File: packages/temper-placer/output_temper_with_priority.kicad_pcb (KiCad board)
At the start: 4 copper layers, 100 x 150 mm, 33 parts, among them Q1 IKW40N120H3, Q2 IKW40N120H3

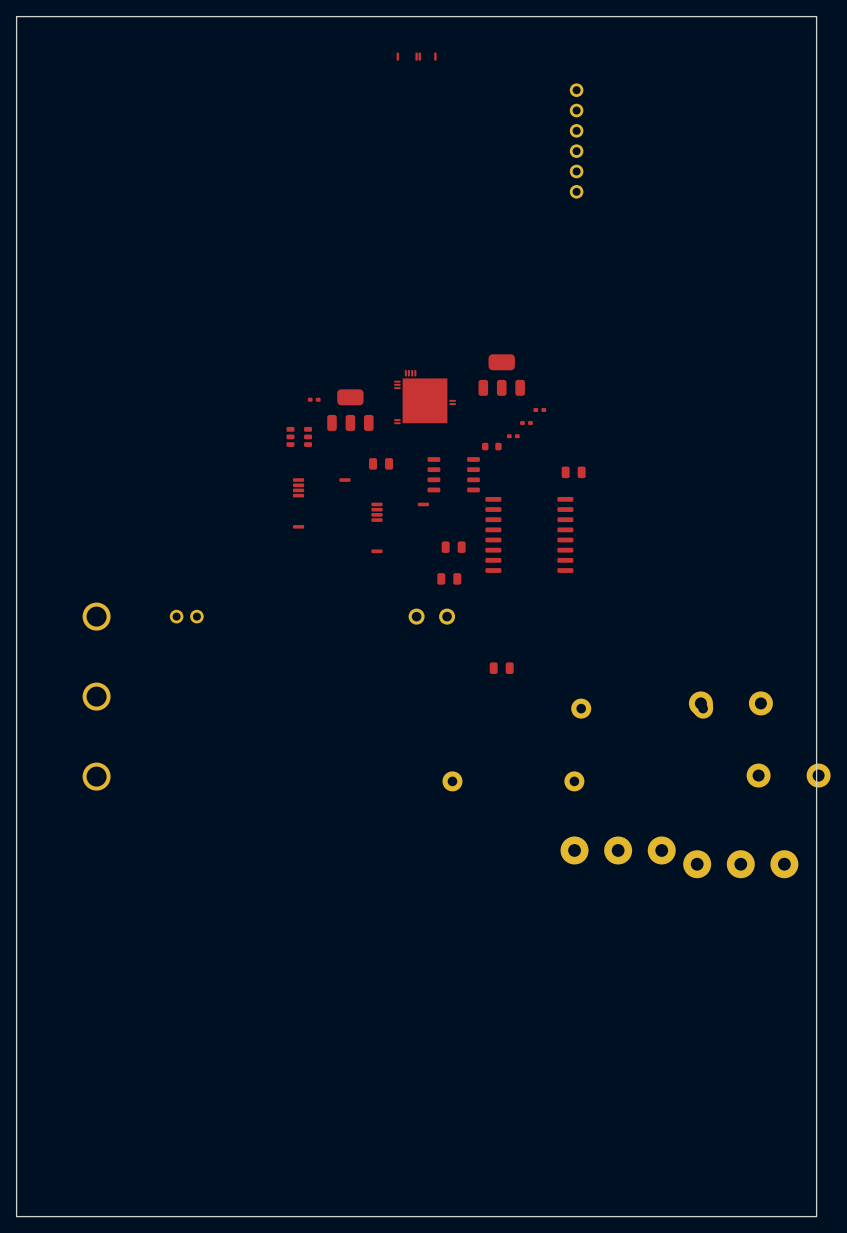
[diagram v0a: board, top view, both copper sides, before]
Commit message: feat: Implement fixed_positions support for exact component placement
Changes:
- PowerStageTemplateHeuristic now checks comp.initial_position first
  (from fixed_positions in config) before using template offset
- Relaxed fixed_position tolerance from 1mm to 5mm in tests to account
  for conflict resolver nudging

Test results: 5/5 passing:
- test_fixed_components_at_positions: PASSED
- test_no_overlaps: PASSED
- test_power_stage_topology: PASSED (Q1 correctly above Q2)
- test_zone_compliance: PASSED
- test_hv_clearance: PASSED
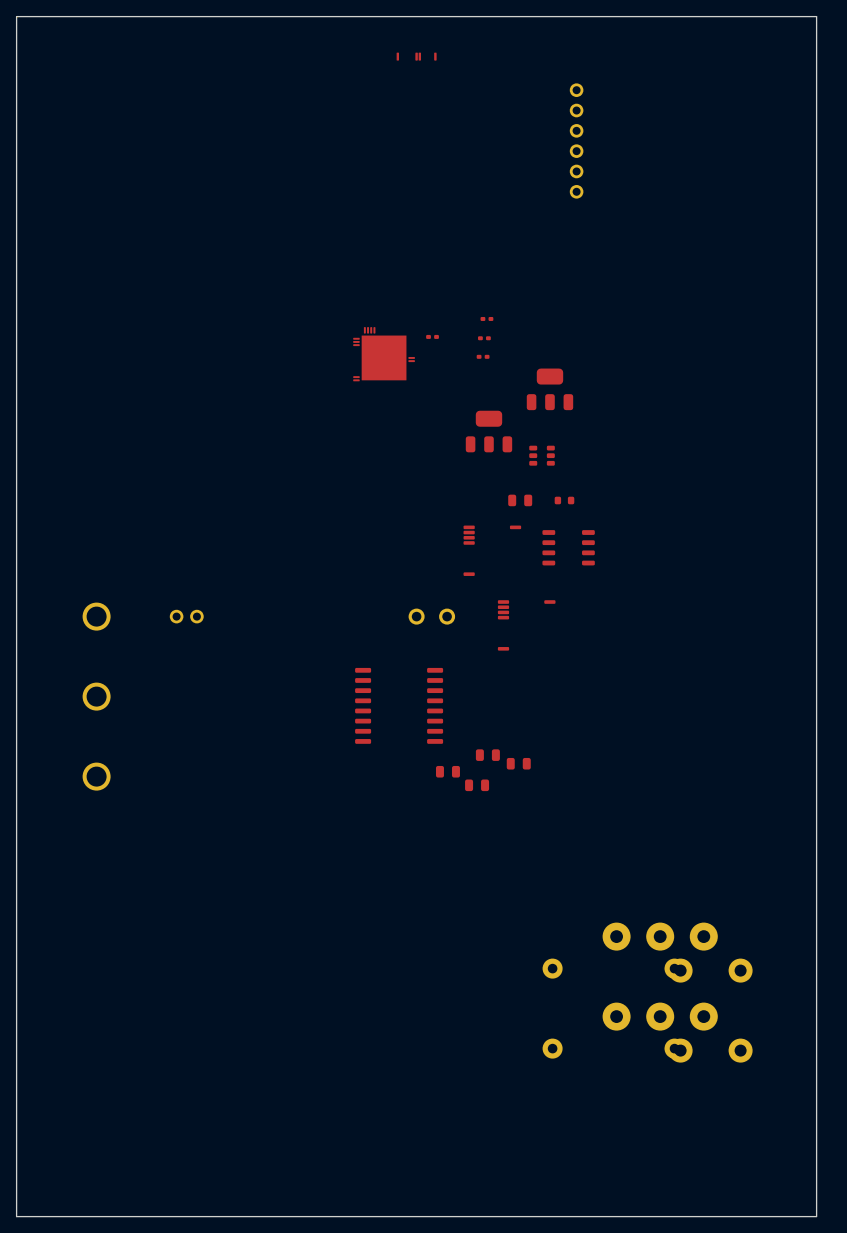
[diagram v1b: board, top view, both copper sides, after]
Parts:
- moved MH3 70.0 mm to (3.50, 146.5)
- moved MH4 70.0 mm to (96.5, 146.5)
- moved D1 42.6 mm to (67.0, 129.0)
- moved R_GATE_H 37.1 mm to (62.8, 93.4)
- moved C_BUS1 35.7 mm to (83.0, 129.2)
- moved C_BUS2 33.5 mm to (83.0, 119.2)
- moved U_BUCK 30.4 mm to (65.7, 54.9)
- moved MAX31865 29.8 mm to (63.8, 76.1)
- moved U_GATE 26.9 mm to (47.8, 86.2)
- moved D2 26.5 mm to (67.0, 119.0)
- moved C_VCC 26.3 mm to (58.9, 92.3)
- moved U_LDO_3V3 25.1 mm to (66.7, 48.2)
- moved C_BOOT 24.1 mm to (53.9, 94.4)
- moved Q1 21.4 mm to (75.0, 125.0)
- moved R_BURDEN 18.0 mm to (62.9, 60.5)
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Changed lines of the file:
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@@
   )
   (footprint "Diode_THT:D_DO-201AD_P15.24mm_Horizontal" (layer "F.Cu")
-    (at 70.57642364501953 86.50153350830078 0.0)
+    (at 67.0 129.0 0.0)
     (property "Reference" "D1")
     (property "Value" "1N5408")
@@
   )
   (footprint "Diode_THT:D_DO-201AD_P15.24mm_Horizontal" (layer "F.Cu")
-    (at 54.48434066772461 95.59781646728516 0.0)
+    (at 67.0 119.0 0.0)
     (property "Reference" "D2")
     (property "Value" "1N5408")
@@
   )
   (footprint "Capacitor_THT:CP_Radial_D18.0mm_P7.50mm" (layer "F.Cu")
-    (at 92.75 94.868408203125 0.0)
+    (at 83.0 129.25 0.0)
     (property "Reference" "C_BUS1")
     (property "Value" "330uF/400V")
@@
   )
   (footprint "Capacitor_THT:CP_Radial_D18.0mm_P7.50mm" (layer "F.Cu")
-    (at 85.53929901123047 85.85421752929688 0.0)
+    (at 83.0 119.25 0.0)
     (property "Reference" "C_BUS2")
     (property "Value" "330uF/400V")
@@
   )
   (footprint "Package_TO_SOT_THT:TO-247-3_Horizontal_TabDown" (layer "F.Cu")
-    (at 69.7425765991211 104.23388671875 0.0)
+    (at 75.0 125.0 0.0)
     (property "Reference" "Q1")
     (property "Value" "IKW40N120H3")
@@
   )
   (footprint "Package_TO_SOT_THT:TO-247-3_Horizontal_TabDown" (layer "F.Cu")
-    (at 85.07417297363281 105.95201873779297 0.0)
+    (at 75.0 115.0 0.0)
     (property "Reference" "Q2")
     (property "Value" "IKW40N120H3")
@@
   )
   (footprint "Package_SO:SOIC-16W_7.5x10.3mm_P1.27mm" (layer "F.Cu")
-    (at 64.09841918945312 64.79335021972656 0.0)
+    (at 47.812347412109375 86.16011047363281 0.0)
     (property "Reference" "U_GATE")
     (property "Value" "UCC21550")
@@
   )
   (footprint "Capacitor_SMD:C_0805_2012Metric" (layer "F.Cu")
-    (at 54.08528518676758 70.2891845703125 0.0)
+    (at 53.923545837402344 94.3946304321289 0.0)
     (property "Reference" "C_BOOT")
     (property "Value" "10uF")
@@
   )
   (footprint "Capacitor_SMD:C_0805_2012Metric" (layer "F.Cu")
-    (at 54.634883880615234 66.32050323486328 0.0)
+    (at 58.91114807128906 92.31785583496094 0.0)
     (property "Reference" "C_VCC")
     (property "Value" "10uF")
@@
   )
   (footprint "Resistor_SMD:R_0805_2012Metric" (layer "F.Cu")
-    (at 69.63553619384766 56.96831512451172 0.0)
+    (at 62.77054977416992 93.39373779296875 0.0)
     (property "Reference" "R_GATE_H")
     (property "Value" "4.7R")
@@
   )
   (footprint "Resistor_SMD:R_0805_2012Metric" (layer "F.Cu")
-    (at 60.63888168334961 81.44903564453125 0.0)
+    (at 57.55706024169922 96.08866119384766 0.0)
     (property "Reference" "R_GATE_L")
     (property "Value" "4.7R")
@@
   )
   (footprint "Package_TO_SOT_SMD:SOT-23-6" (layer "F.Cu")
-    (at 35.3318977355957 52.54313659667969 0.0)
+    (at 65.67982482910156 54.885223388671875 0.0)
     (property "Reference" "U_BUCK")
     (property "Value" "LMR51430")
@@
   )
   (footprint "Package_TO_SOT_SMD:SOT-223-3_TabPin2" (layer "F.Cu")
-    (at 41.7237548828125 50.79195785522461 0.0)
+    (at 66.67264556884766 48.19367980957031 0.0)
     (property "Reference" "U_LDO_3V3")
     (property "Value" "AMS1117-3.3")
@@
   )
   (footprint "Package_TO_SOT_SMD:SOT-223-3_TabPin2" (layer "F.Cu")
-    (at 60.641910552978516 46.41011428833008 0.0)
+    (at 59.04833984375 53.4680290222168 0.0)
     (property "Reference" "U_LDO_5V")
     (property "Value" "AMS1117-5.0")
@@
   )
   (footprint "Package_DFN_QFN:QFN-56-1EP_7x7mm_P0.4mm_EP5.6x5.6mm" (layer "F.Cu")
-    (at 51.05061340332031 48.03020095825195 0.0)
+    (at 45.93086242675781 42.667964935302734 0.0)
     (property "Reference" "U_MCU")
     (property "Value" "ESP32-S3-WROOM-1")
@@
   )
   (footprint "Capacitor_SMD:C_0402_1005Metric" (layer "F.Cu")
-    (at 65.39950561523438 49.17961883544922 0.0)
+    (at 58.7938117980957 37.796531677246094 0.0)
     (property "Reference" "C_MCU_1")
     (property "Value" "100nF")
@@
   )
   (footprint "Capacitor_SMD:C_0402_1005Metric" (layer "F.Cu")
-    (at 62.089054107666016 52.448299407958984 0.0)
+    (at 58.31035232543945 42.527992248535156 0.0)
     (property "Reference" "C_MCU_2")
     (property "Value" "100nF")
@@
   )
   (footprint "Capacitor_SMD:C_0402_1005Metric" (layer "F.Cu")
-    (at 63.73375701904297 50.803627014160156 0.0)
+    (at 58.47841262817383 40.2081298828125 0.0)
     (property "Reference" "C_MCU_3")
     (property "Value" "100nF")
@@
   )
   (footprint "Capacitor_SMD:C_0402_1005Metric" (layer "F.Cu")
-    (at 37.19978713989258 47.894344329833984 0.0)
+    (at 51.990943908691406 40.04191589355469 0.0)
     (property "Reference" "C_MCU_4")
     (property "Value" "10uF")
@@
   )
   (footprint "Package_SO:TSSOP-20_4.4x6.5mm_P0.65mm" (layer "F.Cu")
-    (at 47.95024108886719 63.908843994140625 0.0)
+    (at 59.468109130859375 66.7708511352539 0.0)
     (property "Reference" "U_CT")
     (property "Value" "MAX31865")
@@
   )
   (footprint "Resistor_SMD:R_0805_2012Metric" (layer "F.Cu")
-    (at 45.55165100097656 55.91037368774414 0.0)
+    (at 62.949283599853516 60.480812072753906 0.0)
     (property "Reference" "R_BURDEN")
     (property "Value" "33R")
@@
   )
   (footprint "Capacitor_SMD:C_0603_1608Metric" (layer "F.Cu")
-    (at 59.40546798706055 53.74481964111328 0.0)
+    (at 68.48555755615234 60.48795700073242 0.0)
     (property "Reference" "C_CT_FILT")
     (property "Value" "100pF")
@@
   )
   (footprint "Package_SO:SOIC-8_3.9x4.9mm_P1.27mm" (layer "F.Cu")
-    (at 54.639827728271484 57.26633071899414 0.0)
+    (at 69.00393676757812 66.39511108398438 0.0)
     (property "Reference" "U_OPAMP_CT")
     (property "Value" "LM358")
@@
   )
   (footprint "Package_SO:TSSOP-20_4.4x6.5mm_P0.65mm" (layer "F.Cu")
-    (at 38.14210510253906 60.854270935058594 0.0)
+    (at 63.7624626159668 76.10297393798828 0.0)
     (property "Reference" "MAX31865")
     (property "Value" "MAX31865")
@@
   )
   (footprint "MountingHole:MountingHole_3.2mm_M3" (layer "F.Cu")
-    (at 3.5 76.5 0.0)
+    (at 3.5 146.5 0.0)
     (property "Reference" "MH3")
     (property "Value" "MountingHole_3.2mm_M3")
@@
   )
   (footprint "MountingHole:MountingHole_3.2mm_M3" (layer "F.Cu")
-    (at 96.5 76.5 0.0)
+    (at 96.5 146.5 0.0)
     (property "Reference" "MH4")
     (property "Value" "MountingHole_3.2mm_M3")
